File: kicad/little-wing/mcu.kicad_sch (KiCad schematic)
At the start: 27 parts, among them SW2 Reset, U1 ${ALTIUM_VALUE}, X1 ${ALTIUM_VALUE}, X2 ${ALTIUM_VALUE}

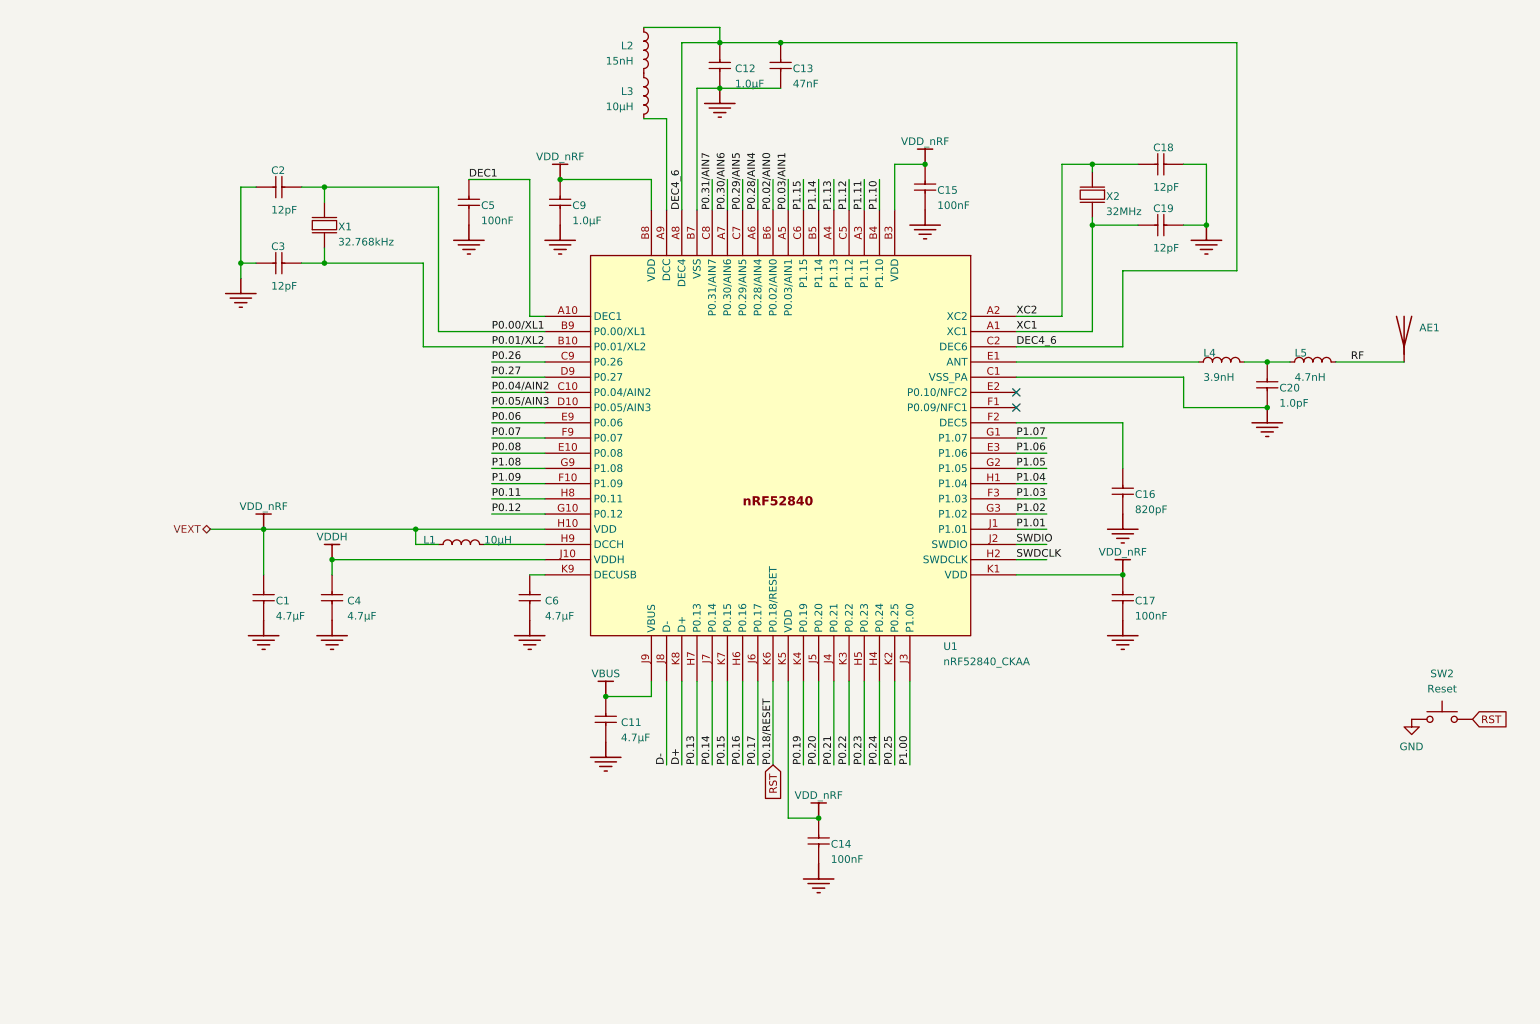
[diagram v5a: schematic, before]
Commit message: Cleaning up the schematics a bit more
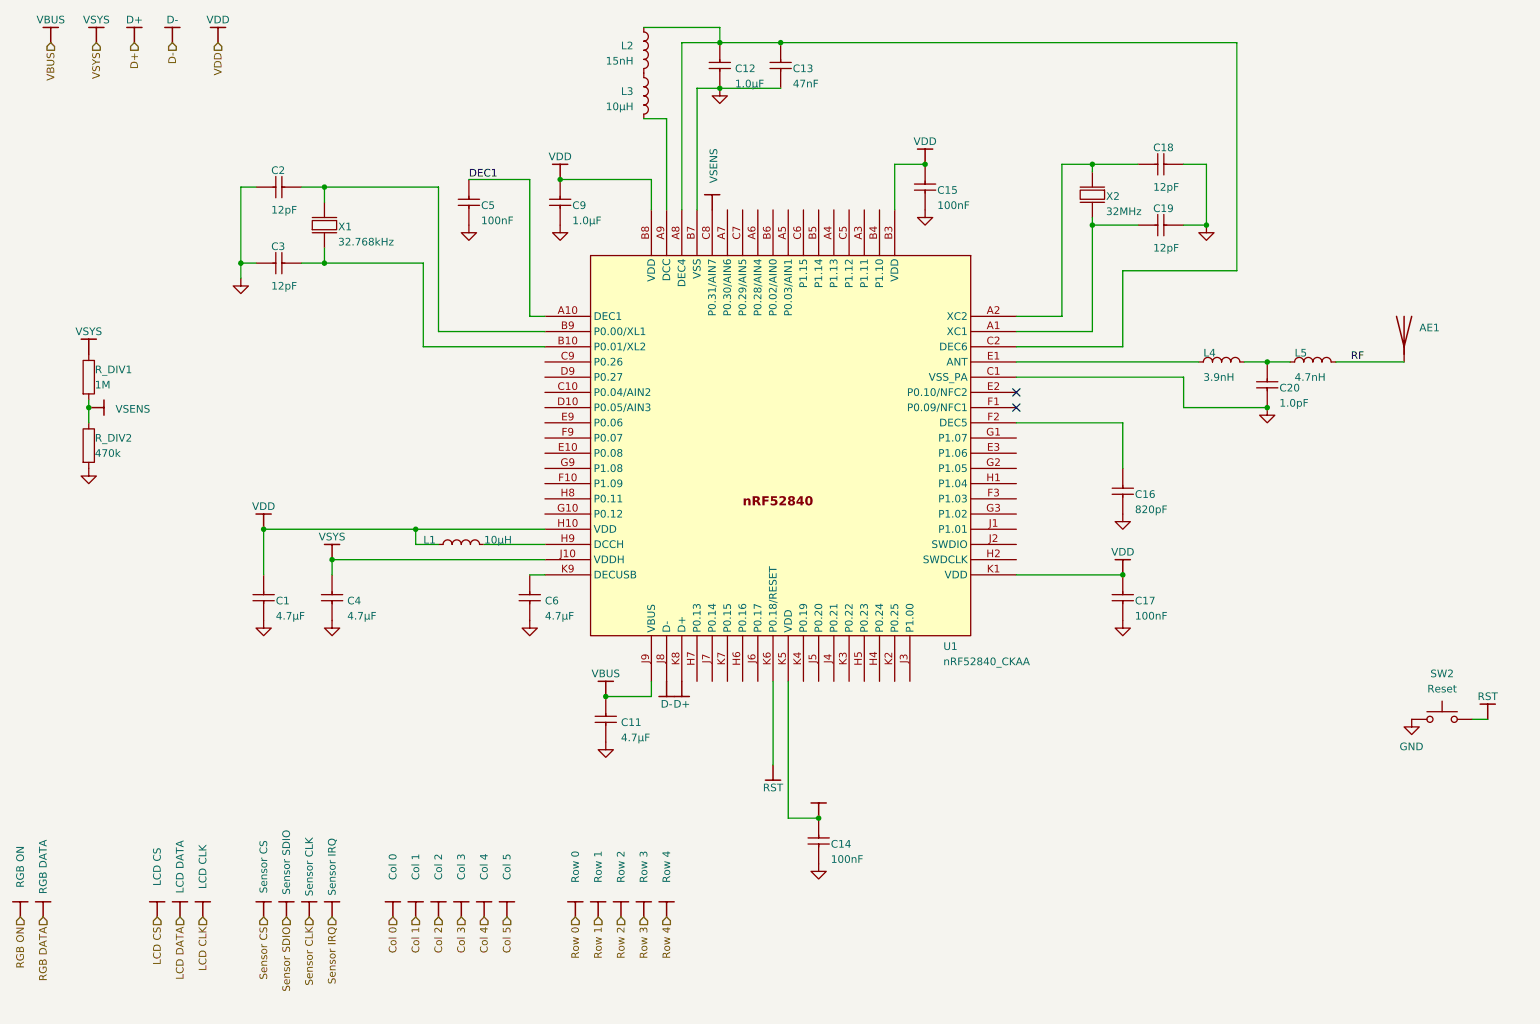
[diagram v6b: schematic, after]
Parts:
- added R_DIV1: 1M, RESC0603X03L_C, symbol AltiumLib:root_3_mirrored_RES_AltiumLib.DbLib
- added R_DIV2: 470k, RESC0603X03L_C, symbol AltiumLib:root_3_mirrored_RES_AltiumLib.DbLib
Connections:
- net GND: now also R_DIV2.2
- net DEC4_6: no longer names the net of C12.2, C13.1, L2.1, U1.A8 (DEC4), U1.C2 (DEC6)
- net P0.00/XL1: no longer names the net of C2.1, U1.B9 (P0.00/XL1), X1.1 (inp)
- net P0.01/XL2: no longer names the net of C3.1, U1.B10 (P0.01/XL2), X1.2 (out)
- net P0.02/AIN0: no longer names the net of U1.B6 (P0.02/AIN0)
- net P0.03/AIN1: no longer names the net of U1.A5 (P0.03/AIN1)
- net P0.04/AIN2: no longer names the net of U1.C10 (P0.04/AIN2)
- net P0.05/AIN3: no longer names the net of U1.D10 (P0.05/AIN3)
- net P0.06: no longer names the net of U1.E9 (P0.06)
- net P0.07: no longer names the net of U1.F9 (P0.07)
- net P0.08: no longer names the net of U1.E10 (P0.08)
- net P0.11: no longer names the net of U1.H8 (P0.11)
- net P0.12: no longer names the net of U1.G10 (P0.12)
- net P0.13: no longer names the net of U1.H7 (P0.13)
- net P0.14: no longer names the net of U1.J7 (P0.14)
- net P0.15: no longer names the net of U1.K7 (P0.15)
- net P0.16: no longer names the net of U1.H6 (P0.16)
- net P0.17: no longer names the net of U1.J6 (P0.17)
- net P0.19: no longer names the net of U1.K4 (P0.19)
- net P0.20: no longer names the net of U1.J5 (P0.20)
- net P0.21: no longer names the net of U1.J4 (P0.21)
- net P0.22: no longer names the net of U1.K3 (P0.22)
- net P0.23: no longer names the net of U1.H5 (P0.23)
- net P0.24: no longer names the net of U1.H4 (P0.24)
- net P0.25: no longer names the net of U1.K2 (P0.25)
- net P0.26: no longer names the net of U1.C9 (P0.26)
- net P0.27: no longer names the net of U1.D9 (P0.27)
- net P0.28/AIN4: no longer names the net of U1.A6 (P0.28/AIN4)
- net P0.29/AIN5: no longer names the net of U1.C7 (P0.29/AIN5)
- net P0.30/AIN6: no longer names the net of U1.A7 (P0.30/AIN6)
- net P0.31/AIN7 renamed VSENS
- net VSENS: now also R_DIV1.2, R_DIV2.1
- net P1.00: no longer names the net of U1.J3 (P1.00)
- net P1.01: no longer names the net of U1.J1 (P1.01)
- net P1.02: no longer names the net of U1.G3 (P1.02)
- net P1.03: no longer names the net of U1.F3 (P1.03)
- net P1.04: no longer names the net of U1.H1 (P1.04)
- net P1.05: no longer names the net of U1.G2 (P1.05)
- net P1.06: no longer names the net of U1.E3 (P1.06)
- net P1.07: no longer names the net of U1.G1 (P1.07)
- net P1.08: no longer names the net of U1.G9 (P1.08)
- net P1.09: no longer names the net of U1.F10 (P1.09)
- net P1.10: no longer names the net of U1.B4 (P1.10)
- net P1.11: no longer names the net of U1.A3 (P1.11)
- net P1.12: no longer names the net of U1.C5 (P1.12)
- net P1.13: no longer names the net of U1.A4 (P1.13)
- net P1.14: no longer names the net of U1.B5 (P1.14)
- net P1.15: no longer names the net of U1.C6 (P1.15)
- net SWDCLK: no longer names the net of U1.H2 (SWDCLK)
- net SWDIO: no longer names the net of U1.J2 (SWDIO)
- net VDDH renamed VSYS
- net VSYS: now also R_DIV1.1
- net VDD_nRF renamed VDD
- net XC1: no longer names the net of C19.1, U1.A1 (XC1), X2.1 (inp)
- net XC2: no longer names the net of C18.1, U1.A2 (XC2), X2.3 (out)

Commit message: Updating schematics/pcb to match the labels
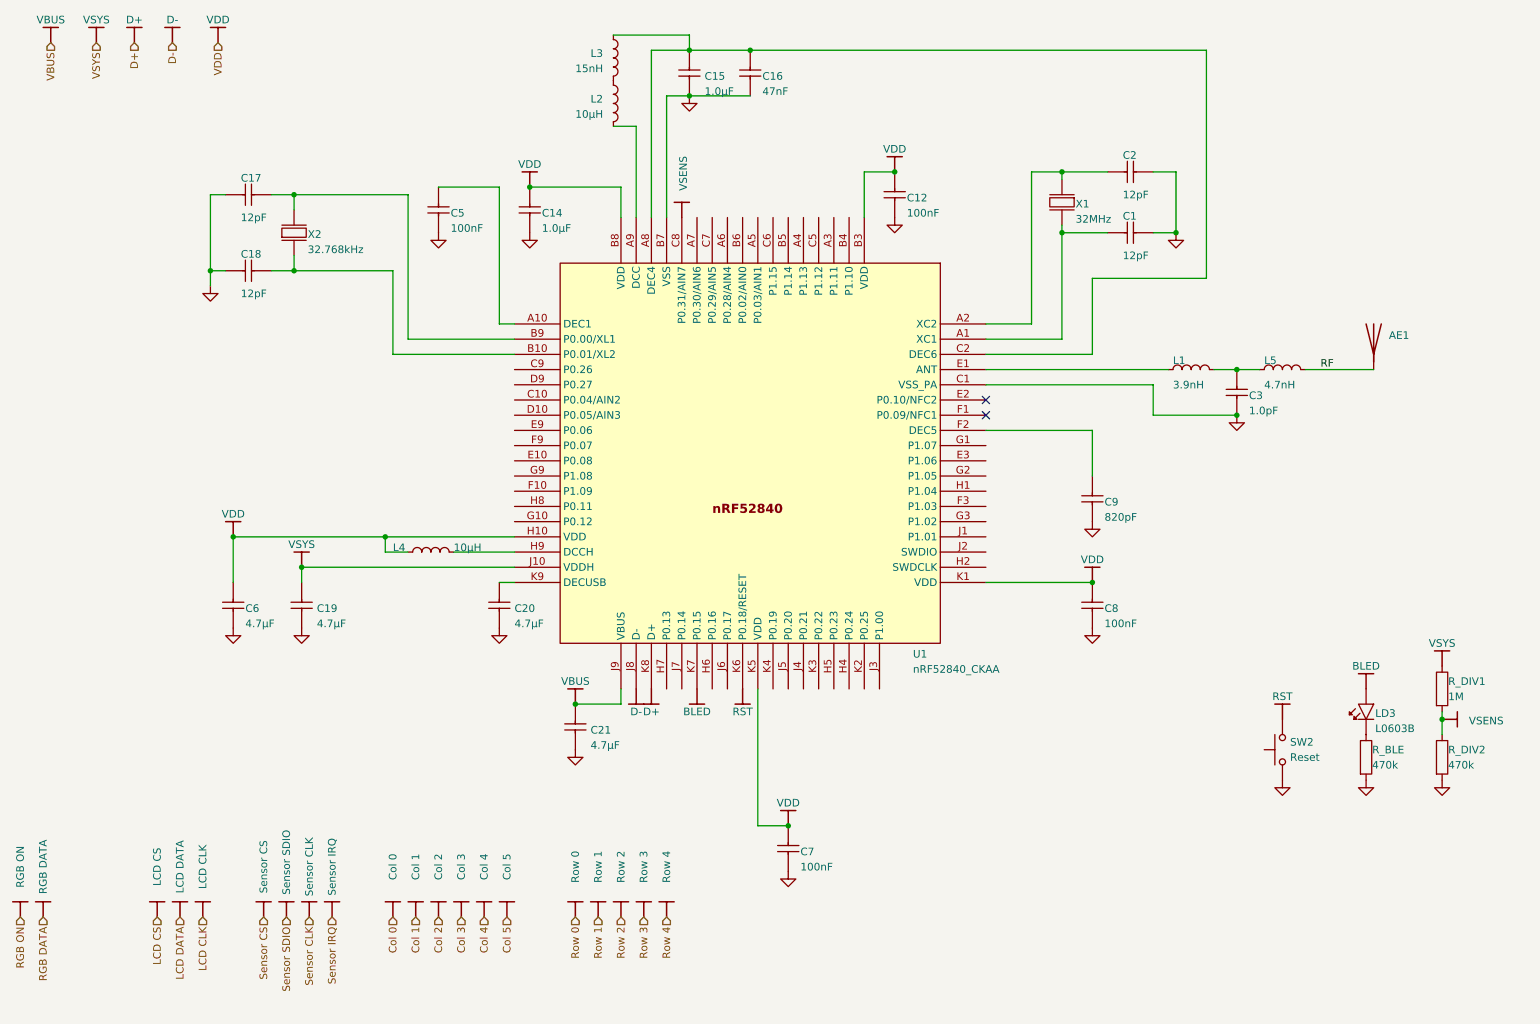
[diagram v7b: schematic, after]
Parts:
- removed C1, C11, C4: ${ALTIUM_VALUE}, CAPC1608X06L, symbol Nordic Passive DB:root_3_CAP_Nordic Passive DB.DbLib
- removed C12: ${ALTIUM_VALUE}, CAPC1608X06L, symbol Nordic Passive DB:root_1_CAP_Nordic Passive DB.DbLib
- removed C13, C15, C17: ${ALTIUM_VALUE}, CAPC0603X03L_C, symbol Nordic Passive DB:root_3_CAP_Nordic Passive DB.DbLib
- removed C18, C19: ${ALTIUM_VALUE}, CAPC0603X03L_C, symbol Nordic Passive DB:root_0_CAP_Nordic Passive DB.DbLib
- removed C2, C3: ${ALTIUM_VALUE}, CAPC0603X03L_C, symbol Nordic Passive DB:root_2_CAP_Nordic Passive DB.DbLib
- removed C20: ${ALTIUM_VALUE}, CAPC0603X03L_C, symbol Nordic Passive DB:root_1_CAP_Nordic Passive DB.DbLib
- removed X1: ${ALTIUM_VALUE}, XTAL_2012, symbol Nordic Discrete DB:root_3_XTAL_2-pin_Nordic Discrete DB.DbLib
- removed X2: ${ALTIUM_VALUE}, BT-XTAL_2016, symbol Nordic Discrete DB:root_1_XTAL_4-pin_grounded_Nordic Discrete DB.DbLib
- added C1, C2: ${ALTIUM_VALUE}, CAPC0603X03L_C, symbol Nordic Passive DB:root_0_CAP_Nordic Passive DB.DbLib
- added C12, C7, C8: ${ALTIUM_VALUE}, CAPC0603X03L_C, symbol Nordic Passive DB:root_3_CAP_Nordic Passive DB.DbLib
- added C15: ${ALTIUM_VALUE}, CAPC1608X06L, symbol Nordic Passive DB:root_1_CAP_Nordic Passive DB.DbLib
- added C17, C18: ${ALTIUM_VALUE}, CAPC0603X03L_C, symbol Nordic Passive DB:root_2_CAP_Nordic Passive DB.DbLib
- added C19, C20, C21: ${ALTIUM_VALUE}, CAPC1608X06L, symbol Nordic Passive DB:root_3_CAP_Nordic Passive DB.DbLib
- added C3: ${ALTIUM_VALUE}, CAPC0603X03L_C, symbol Nordic Passive DB:root_1_CAP_Nordic Passive DB.DbLib
- added LD3: L0603B, LED_0603_R, symbol AltiumLib:root_3_mirrored_D{colon}LED_AltiumLib.DbLib
- added R_BLE: 470k, RESC0603X03L_C, symbol AltiumLib:root_3_mirrored_RES_AltiumLib.DbLib
- added X1: ${ALTIUM_VALUE}, BT-XTAL_2016, symbol Nordic Discrete DB:root_1_XTAL_4-pin_grounded_Nordic Discrete DB.DbLib
- added X2: ${ALTIUM_VALUE}, XTAL_2012, symbol Nordic Discrete DB:root_3_XTAL_2-pin_Nordic Discrete DB.DbLib
- C14: footprint CAPC0603X03L_C -> CAPC1608X06L; ALTIUM_VALUE 100nF -> 1.0µF; FOOTPRINT DOC 0201 -> 0603; LATESTREVISIONDATE 2017-11-09 -> 2013-06-05; PART NUMBER C0201-100n -> C0603-1µ0; PUBLISHED 2014-11-13 -> 2009-05-08
- C16: ALTIUM_VALUE 820pF -> 47nF; PART NUMBER C0201-820p -> C0201-47n
- C9: footprint CAPC1608X06L -> CAPC0603X03L_C; ALTIUM_VALUE 1.0µF -> 820pF; FOOTPRINT DOC 0603 -> 0201; LATESTREVISIONDATE 2013-06-05 -> 2017-11-09; PART NUMBER C0603-1µ0 -> C0201-820p; PUBLISHED 2009-05-08 -> 2014-11-13
- L1: footprint INDC1608X06L -> INDC0603X03L_C; ALTIUM_VALUE 10µH -> 3.9nH; FOOTPRINT DOC 0603 -> 0201; LATESTREVISIONDATE 2012-09-19 -> 2017-11-09; MANUFACTURER (none) -> *; MANUFACTURER PART NUMBER (none) -> *; PART NUMBER L0603-10µ -> L0201-3n9; PUBLISHED 2010-02-24 -> 2013-04-10
- L2: footprint INDC1005X04L -> INDC1608X06L; ALTIUM_VALUE 15nH -> 10µH; FOOTPRINT DOC 0402 -> 0603; PART NUMBER L0402-15n -> L0603-10µ; PUBLISHED 2010-07-12 -> 2010-02-24
- L3: footprint INDC1608X06L -> INDC1005X04L; ALTIUM_VALUE 10µH -> 15nH; FOOTPRINT DOC 0603 -> 0402; PART NUMBER L0603-10µ -> L0402-15n; PUBLISHED 2010-02-24 -> 2010-07-12
- L4: footprint INDC0603X03L_C -> INDC1608X06L; ALTIUM_VALUE 3.9nH -> 10µH; FOOTPRINT DOC 0201 -> 0603; LATESTREVISIONDATE 2017-11-09 -> 2012-09-19; MANUFACTURER * -> (none); MANUFACTURER PART NUMBER * -> (none); PART NUMBER L0201-3n9 -> L0603-10µ; PUBLISHED 2013-04-10 -> 2010-02-24
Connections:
- net GND: now also C1.2, C12.2, C15.1, C17.2, C18.2, C19.2, C2.2, C20.2, C21.2, C3.1, C7.2, C8.2, R_BLE.2
- net VBUS: now also C21.1
- net VDD: now also C6.1, L4.1, C12.1, C7.1, C8.1; no longer C9.1, L1.1
- net VSYS: now also C19.1
- net at L4.2: now also U1.H9 (DCCH); no longer L5.1
- net at U1.A8 (DEC4), U1.C2 (DEC6): now also C16.1, L3.1, C15.2; no longer L2.1
- net at L2.2: now also U1.A9 (DCC); no longer L3.1
- net at U1.A1 (XC1): now also C1.1, X1.1 (inp)
- net at U1.A2 (XC2): now also C2.1, X1.3 (out)
- net at L3.2: now also L2.1; no longer U1.A9 (DCC)
- net at U1.B10 (P0.01/XL2): now also C18.1, X2.2 (out)
- net at U1.B9 (P0.00/XL1): now also C17.1, X2.1 (inp)
- net at U1.E1 (ANT): now also L1.1; no longer L4.1
- net at U1.F2 (DEC5): now also C9.1; no longer C16.1
- net at L1.2: now also L5.1, C3.2; no longer U1.H9 (DCCH)
- net BLED: now reaches U1.K7 (P0.15)
- net BLED: now also LD3.2 (A)
- net at U1.K9 (DECUSB): now also C20.1; no longer C6.1
- net DEC1: no longer names the net of C5.1, U1.A10 (DEC1)
- new net: LD3.1 (C), R_BLE.1
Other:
- moved on the sheet: AE1, R_DIV1, R_DIV2, SW2

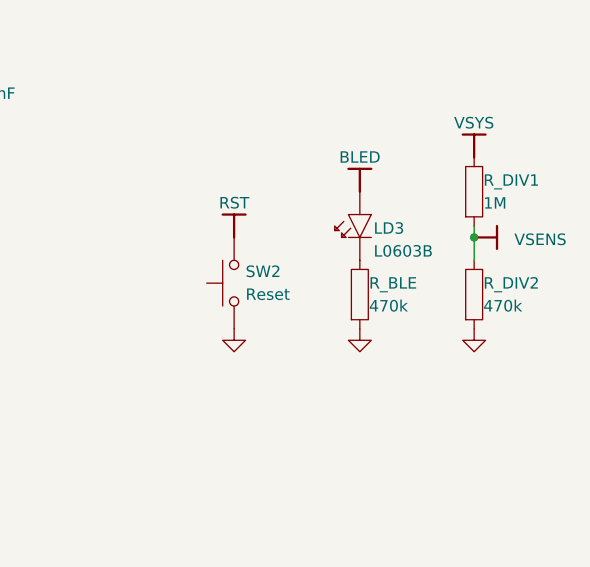
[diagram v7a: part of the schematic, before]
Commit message: Cleaning up some space on the PCB
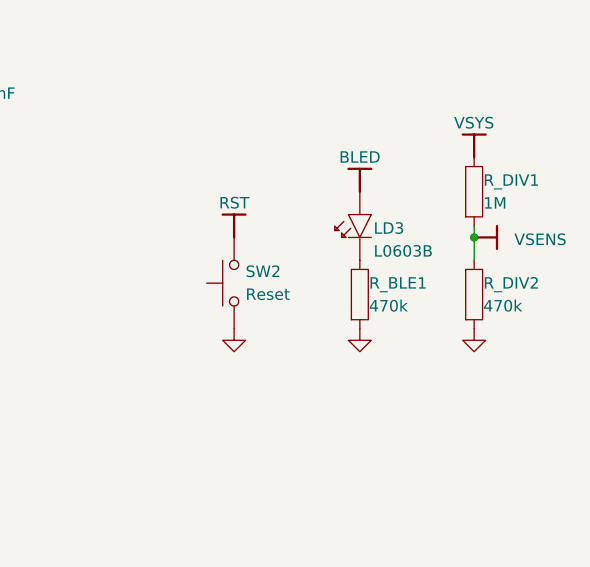
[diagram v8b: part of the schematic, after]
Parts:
- renumbered R_BLE to R_BLE1
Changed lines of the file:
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@@
 		(on_board yes)
 		(dnp no)
-		(property "Reference" "R_BLE"
+		(property "Reference" "R_BLE1"
 			(at 249.936 145.542 0)
 			(effects
@@
 			(project "little-wing"
 				(path "/3a835e6f-a660-4b38-a102-87841cdd95ed/eaaf4618-ba3d-41b4-8a99-4f719e243661/ebcf195d-f1fd-431a-a78e-86a1a85cb647"
-					(reference "R_BLE")
+					(reference "R_BLE1")
 					(unit 1)
 				)
